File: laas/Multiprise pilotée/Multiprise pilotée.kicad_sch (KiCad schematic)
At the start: 0 parts

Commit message: Sauvegarde du travail en cours
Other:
- sheet DC supplies ports: added CS_PWR_DC, LATCH, MOSI, PWM_PWR_VAR, SCLK, ~{RESET_IO}; removed none
- sheet MCU ports: added CS_PWR_DC, LATCH, PWM_VAR_PWR, SPI_MOSI, SPI_SCK, ~{CS_RELAY}, ~{RESET_IO}; removed none
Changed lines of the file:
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@@
 (kicad_sch (version 20230121) (generator eeschema)
   (paper "A4")
-  (sheet (at 149.86 106.68) (size 54.61 29.21) (fields_autoplaced)
+  (junction (at 127 102.87) (diameter 0) (color 0 0 0 0)
+  )
+  (junction (at 124.46 100.33) (diameter 0) (color 0 0 0 0)
+  )
+  (junction (at 121.92 86.36) (diameter 0) (color 0 0 0 0)
+  )
+  (wire (pts (xy 134.62 81.28) (xy 134.62 44.45))
+    (stroke (width 0) (type default))
+  )
+  (wire (pts (xy 115.57 88.9) (xy 119.38 88.9))
+    (stroke (width 0) (type default))
+  )
+  (wire (pts (xy 134.62 44.45) (xy 115.57 44.45))
+    (stroke (width 0) (type default))
+  )
+  (wire (pts (xy 124.46 137.16) (xy 124.46 100.33))
+    (stroke (width 0) (type default))
+  )
+  (wire (pts (xy 127 102.87) (xy 127 139.7))
+    (stroke (width 0) (type default))
+  )
+  (wire (pts (xy 119.38 97.79) (xy 115.57 97.79))
+    (stroke (width 0) (type default))
+  )
+  (wire (pts (xy 119.38 54.61) (xy 115.57 54.61))
+    (stroke (width 0) (type default))
+  )
+  (wire (pts (xy 127 139.7) (xy 115.57 139.7))
+    (stroke (width 0) (type default))
+  )
+  (wire (pts (xy 115.57 123.19) (xy 121.92 123.19))
+    (stroke (width 0) (type default))
+  )
+  (wire (pts (xy 129.54 95.25) (xy 129.54 60.96))
+    (stroke (width 0) (type default))
+  )
+  (wire (pts (xy 115.57 137.16) (xy 124.46 137.16))
+    (stroke (width 0) (type default))
+  )
+  (wire (pts (xy 115.57 95.25) (xy 129.54 95.25))
+    (stroke (width 0) (type default))
+  )
+  (wire (pts (xy 119.38 88.9) (xy 119.38 54.61))
+    (stroke (width 0) (type default))
+  )
+  (wire (pts (xy 119.38 134.62) (xy 119.38 97.79))
+    (stroke (width 0) (type default))
+  )
+  (wire (pts (xy 115.57 102.87) (xy 127 102.87))
+    (stroke (width 0) (type default))
+  )
+  (wire (pts (xy 127 66.04) (xy 127 102.87))
+    (stroke (width 0) (type default))
+  )
+  (wire (pts (xy 115.57 134.62) (xy 119.38 134.62))
+    (stroke (width 0) (type default))
+  )
+  (wire (pts (xy 129.54 60.96) (xy 115.57 60.96))
+    (stroke (width 0) (type default))
+  )
+  (wire (pts (xy 115.57 100.33) (xy 124.46 100.33))
+    (stroke (width 0) (type default))
+  )
+  (wire (pts (xy 124.46 63.5) (xy 115.57 63.5))
+    (stroke (width 0) (type default))
+  )
+  (wire (pts (xy 115.57 86.36) (xy 121.92 86.36))
+    (stroke (width 0) (type default))
+  )
+  (wire (pts (xy 115.57 66.04) (xy 127 66.04))
+    (stroke (width 0) (type default))
+  )
+  (wire (pts (xy 124.46 100.33) (xy 124.46 63.5))
+    (stroke (width 0) (type default))
+  )
+  (wire (pts (xy 115.57 81.28) (xy 134.62 81.28))
+    (stroke (width 0) (type default))
+  )
+  (wire (pts (xy 121.92 123.19) (xy 121.92 86.36))
+    (stroke (width 0) (type default))
+  )
+  (wire (pts (xy 121.92 86.36) (xy 121.92 52.07))
+    (stroke (width 0) (type default))
+  )
+  (wire (pts (xy 121.92 52.07) (xy 115.57 52.07))
+    (stroke (width 0) (type default))
+  )
+  (sheet (at 58.42 77.47) (size 57.15 29.21) (fields_autoplaced)
     (stroke (width 0.1524) (type solid))
     (fill (color 0 0 0 0.0000))
-    (property "Sheetname" "MCU" (at 149.86 105.9684 0)
+    (property "Sheetname" "MCU" (at 58.42 76.7584 0)
       (effects (font (size 1.27 1.27)) (justify left bottom))
     )
-    (property "Sheetfile" "Mcu.kicad_sch" (at 149.86 136.4746 0)
+    (property "Sheetfile" "Mcu.kicad_sch" (at 58.42 107.2646 0)
       (effects (font (size 1.27 1.27)) (justify left top))
+    )
+    (pin "SPI_MOSI" input (at 115.57 102.87 0)
+      (effects (font (size 1.27 1.27)) (justify right))
+    )
+    (pin "SPI_SCK" input (at 115.57 100.33 0)
+      (effects (font (size 1.27 1.27)) (justify right))
+    )
+    (pin "~{CS_RELAY}" input (at 115.57 97.79 0)
+      (effects (font (size 1.27 1.27)) (justify right))
+    )
+    (pin "CS_PWR_DC" input (at 115.57 95.25 0)
+      (effects (font (size 1.27 1.27)) (justify right))
+    )
+    (pin "LATCH" input (at 115.57 88.9 0)
+      (effects (font (size 1.27 1.27)) (justify right))
+    )
+    (pin "~{RESET_IO}" input (at 115.57 86.36 0)
+      (effects (font (size 1.27 1.27)) (justify right))
+    )
+    (pin "PWM_VAR_PWR" input (at 115.57 81.28 0)
+      (effects (font (size 1.27 1.27)) (justify right))
     )
     (instances
@@
     )
   )
-  (sheet (at 58.42 43.18) (size 57.15 30.48) (fields_autoplaced)
+  (sheet (at 58.42 40.64) (size 57.15 30.48) (fields_autoplaced)
     (stroke (width 0.1524) (type solid))
     (fill (color 0 0 0 0.0000))
-    (property "Sheetname" "DC supplies" (at 58.42 42.4684 0)
+    (property "Sheetname" "DC supplies" (at 58.42 39.9284 0)
       (effects (font (size 1.27 1.27)) (justify left bottom))
     )
-    (property "Sheetfile" "DC_supplies.kicad_sch" (at 58.42 74.2446 0)
+    (property "Sheetfile" "DC_supplies.kicad_sch" (at 58.42 71.7046 0)
       (effects (font (size 1.27 1.27)) (justify left top))
+    )
+    (pin "PWM_PWR_VAR" input (at 115.57 44.45 0)
+      (effects (font (size 1.27 1.27)) (justify right))
+    )
+    (pin "~{RESET_IO}" input (at 115.57 52.07 0)
+      (effects (font (size 1.27 1.27)) (justify right))
+    )
+    (pin "SCLK" input (at 115.57 63.5 0)
+      (effects (font (size 1.27 1.27)) (justify right))
+    )
+    (pin "MOSI" input (at 115.57 66.04 0)
+      (effects (font (size 1.27 1.27)) (justify right))
+    )
+    (pin "LATCH" input (at 115.57 54.61 0)
+      (effects (font (size 1.27 1.27)) (justify right))
+    )
+    (pin "CS_PWR_DC" input (at 115.57 60.96 0)
+      (effects (font (size 1.27 1.27)) (justify right))
     )
     (instances
@@
     )
   )
-  (sheet (at 151.13 43.18) (size 55.88 30.48) (fields_autoplaced)
+  (sheet (at 58.42 113.03) (size 57.15 30.48) (fields_autoplaced)
     (stroke (width 0.1524) (type solid))
     (fill (color 0 0 0 0.0000))
-    (property "Sheetname" "Power supply and relays" (at 151.13 42.4684 0)
+    (property "Sheetname" "Power supply and relays" (at 58.42 112.3184 0)
       (effects (font (size 1.27 1.27)) (justify left bottom))
     )
-    (property "Sheetfile" "Power.kicad_sch" (at 151.13 74.2446 0)
+    (property "Sheetfile" "Power.kicad_sch" (at 58.42 144.0946 0)
       (effects (font (size 1.27 1.27)) (justify left top))
     )
-    (pin "~{CS_Relay}" input (at 207.01 52.07 0)
+    (pin "~{CS_Relay}" input (at 115.57 134.62 0)
       (effects (font (size 1.27 1.27)) (justify right))
     )
-    (pin "SCLK" input (at 207.01 55.88 0)
+    (pin "SCLK" input (at 115.57 137.16 0)
       (effects (font (size 1.27 1.27)) (justify right))
     )
-    (pin "~{RESET_IO}" input (at 207.01 59.69 0)
+    (pin "~{RESET_IO}" input (at 115.57 123.19 0)
       (effects (font (size 1.27 1.27)) (justify right))
     )
-    (pin "MOSI" input (at 207.01 63.5 0)
+    (pin "MOSI" input (at 115.57 139.7 0)
       (effects (font (size 1.27 1.27)) (justify right))
     )

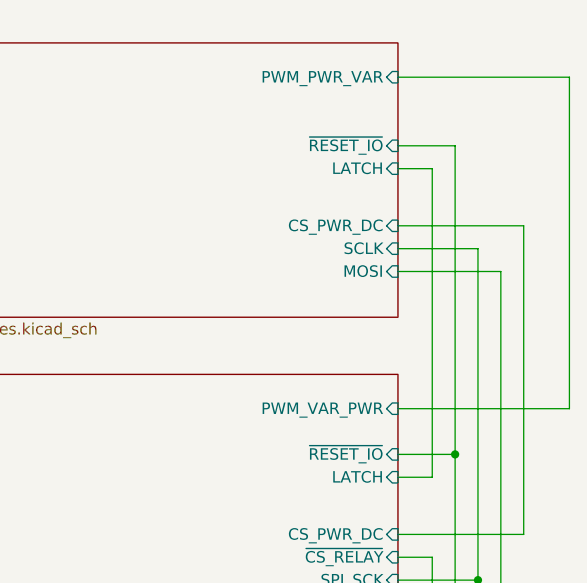
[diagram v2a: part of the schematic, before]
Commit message: Nouvelle version PCB multiprise 1.3 avec suppresion des alim vpol et var
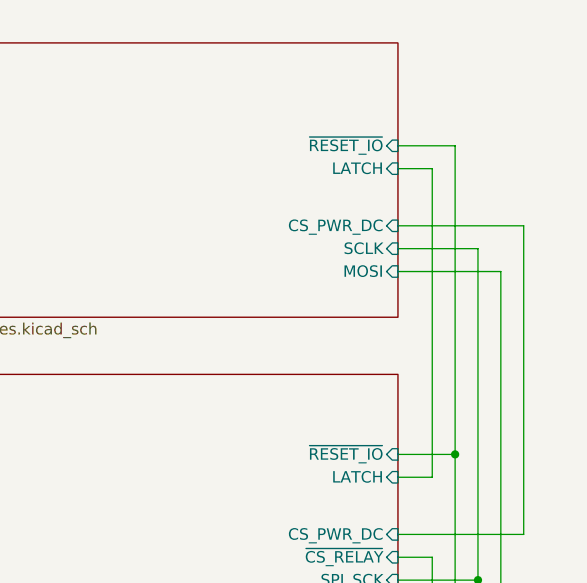
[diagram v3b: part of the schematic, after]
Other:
- sheet DC supplies ports: added none; removed PWM_PWR_VAR
- sheet MCU ports: added none; removed PWM_VAR_PWR
- company: (none) -> INSA - GEI
- title: (none) -> Multiprise
